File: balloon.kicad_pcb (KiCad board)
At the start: 2 copper layers, 100 x 100 mm, 94 parts, among them J1 USB_B_Micro, J2 Conn_01x06_Socket, J3 Conn_01x06_Socket, J4 Conn_01x02_Socket, J5 Writing Connector, J6 Micro_SD_Card_Det_Hirose_DM3AT, Q1 BSS138, Q2 2SJ681, Q3 BSS138, SW1 DTS-63-F-N-V-RED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

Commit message: replace PCB
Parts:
- removed REF** (x3): MountingHole_3.2mm_M3, MountingHole:MountingHole_3.2mm_M3
- added G***: LOGO, balloon:PQ_LOGO, B.Cu at (53.2, 64.2)
- added H1: MountingHole, MountingHole:MountingHole_3.2mm_M3_ISO7380, F.Cu at (27.8, 49.9)
- added H2: MountingHole, MountingHole:MountingHole_3.2mm_M3_ISO7380, F.Cu at (27.8, 141.5)
- added H3: MountingHole, MountingHole:MountingHole_3.2mm_M3_ISO7380, F.Cu at (119.6, 50.0)
- added J7: Conn_01x06_Socket, Connector_PinHeader_2.54mm:PinHeader_1x06_P2.54mm_Vertical, F.Cu at (45.6, 143.7)
- added J8: Bypass, Connector_PinSocket_2.54mm:PinSocket_1x02_P2.54mm_Vertical, F.Cu at (88.4, 50.5)
- U1: footprint Package_SO:MSOP-10_3x3mm_P0.5mm -> Package_SO:SOP-8_3.9x4.9mm_P1.27mm
- moved J5 55.4 mm to (27.1, 86.3)
- moved J3 17.5 mm to (64.4, 143.7), turned to -90 degrees
- moved J2 14.3 mm to (61.9, 137.3), turned to -90 degrees
- moved C1 1.88 mm to (38.8, 122.7)
- moved U1 0.94 mm to (33.8, 123.7)
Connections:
- J2 pad 3: /PB12 -> /PA0
- J2 pad 4: /PB13 -> /PA7
- J2 pad 5: /PB14 -> /PB0
- J2 pad 6: /PB15 -> GND1
- J3 pad 1: /PC0 -> /I2C3_SDA
- J3 pad 2: /PC1 -> /I2C3_SCL
- J3 pad 3: /PA0 -> unconnected-(J3-Pin_3-Pad3)
- J3 pad 4: /PA7 -> unconnected-(J3-Pin_4-Pad4)
- J3 pad 5: /PA15 -> GND1
- J3 pad 6: /PB0 -> +3V3
- U5 pad 33: /PB12 -> /SPI2_NSS
- U5 pad 34: /PB13 -> /SPI2_SCK
- U5 pad 35: /PB14 -> /SPI2_MISO
- U5 pad 36: /PB15 -> /SPI2_MOSI
- U5 pad 8: /PC0 -> /I2C3_SCL
- U5 pad 9: /PC1 -> /I2C3_SDA
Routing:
- net GND1: track 603.2 -> 0.00 mm, vias 245 -> 303
- net /USART3_TX: track 79.9 -> 161.3 mm
- net /SWCLK: track 10.2 -> 86.6 mm, vias 0 -> 2
- net /SWO: track 17.5 -> 72.2 mm, vias 0 -> 1
- net /I2C3_SCL: track 0.00 -> 54.4 mm, vias 0 -> 2
- net /SWDIO: track 21.5 -> 72.1 mm, vias 1 -> 3
- net +3V3: track 191.4 -> 240.8 mm, vias 1 -> 3
- net /SPI2_SCK: track 0.00 -> 47.5 mm, vias 0 -> 1
- net /BOOT0: track 57.1 -> 103.0 mm, vias 2 -> 1
- net /PC0: track 45.6 -> 0.00 mm, vias 1 -> 0
- net Net-(BT2--): track 18.5 -> 61.8 mm, vias 0 -> 1
- net /PC1: track 42.9 -> 0.00 mm, vias 1 -> 0
- net /I2C3_SDA: track 0.00 -> 42.3 mm, vias 0 -> 2
- net /USART3_RX: track 86.4 -> 128.6 mm, vias 2 -> 1
- net /SPI2_NSS: track 0.00 -> 37.7 mm, vias 0 -> 1
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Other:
- board text added: "1"
- board text added: "2024 PQ-Balloon"
- board text added: "3V3"
- board text added: "AE_BNO280"
- board text added: "BNO055"
- board text added: "DNP"
- board text added: "GND"
- board text added: "GNSS"
- board text added: "MISO"
- board text added: "MOSI"
- board text added: "NRST"
- board text added: "ON"
- board text added: "RM92"
- board text added: "SCL"
- board text added: "SDA"
- board text added: "SS"
- board text added: "SWCLK"
- board text added: "SWDIO"
- board text added: "SWO"

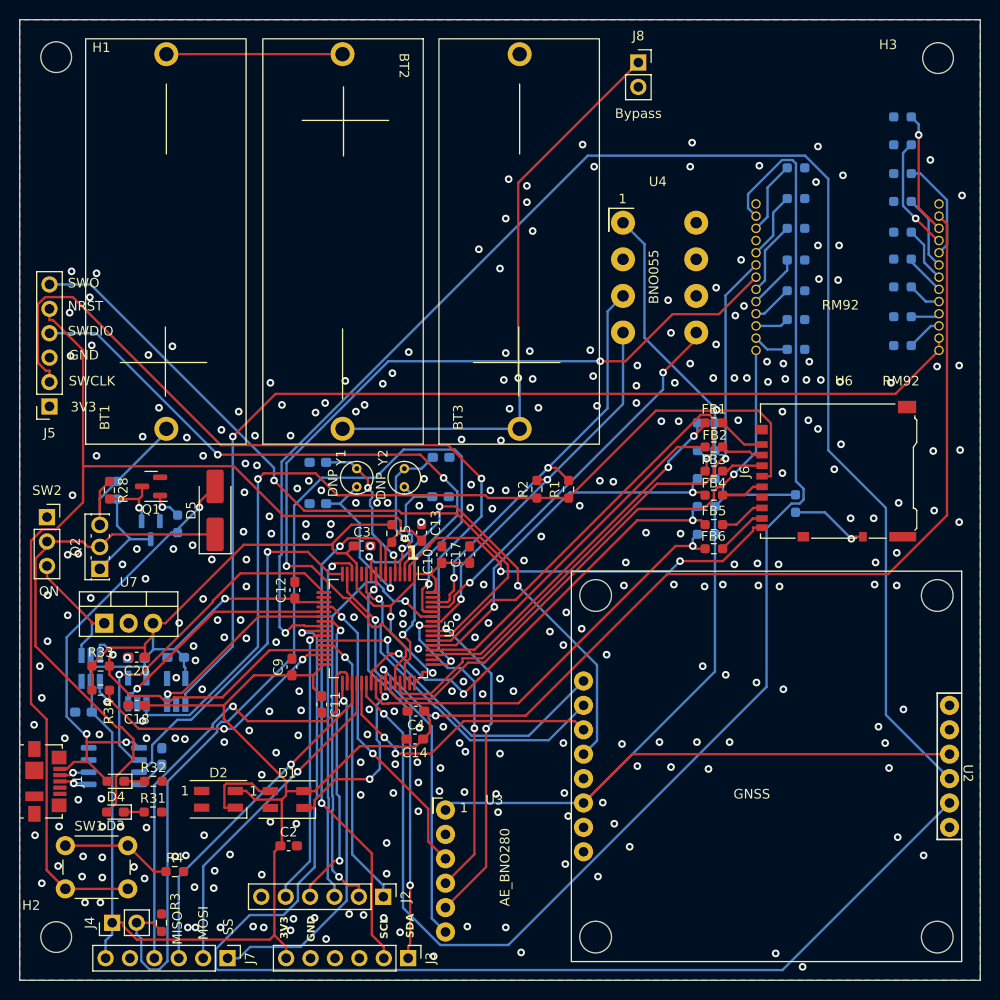
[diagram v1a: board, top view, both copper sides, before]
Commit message: add stmcube
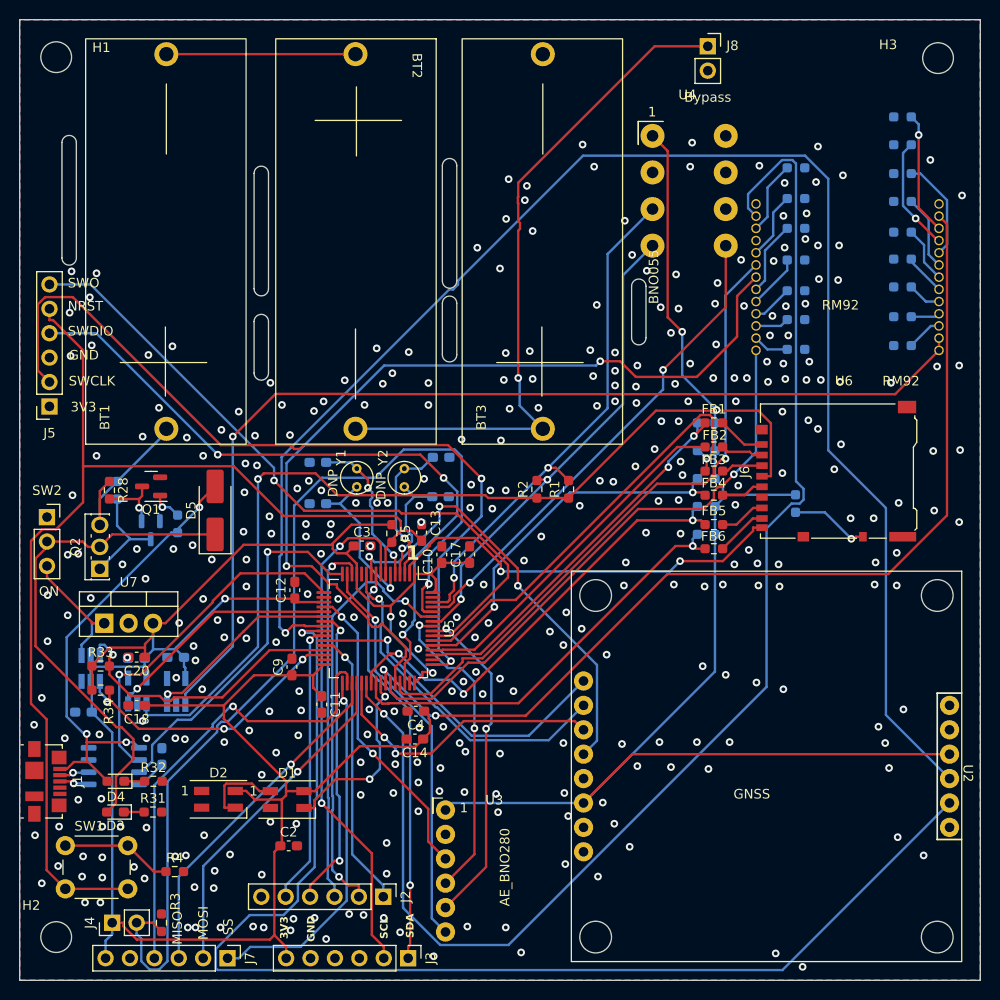
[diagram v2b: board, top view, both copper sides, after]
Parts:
- moved G*** 70.1 mm to (103.2, 113.3), turned to 90 degrees
- moved U4 9.55 mm to (93.6, 63.0)
- moved J8 7.43 mm to (95.6, 48.8)
- moved BT3 2.41 mm to (78.4, 69.2)
- moved BT2 1.35 mm to (59.1, 69.0)
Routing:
- net /I2C1_SDA: track 43.6 -> 54.0 mm
- net /I2C1_SCL: track 39.9 -> 50.2 mm
- net /BNO055_RESET: track 41.0 -> 51.3 mm
- net Net-(BT2--): track 61.8 -> 72.0 mm
- net /PowerSource/VSENSE: track 232.0 -> 239.8 mm, vias 2 -> 3
- net /USART1_CTS: track 88.2 -> 92.2 mm
- net Net-(BT1--): track 18.3 -> 19.7 mm
- net /USART3_TX: track 161.3 -> 161.8 mm
- net GND1: vias 303 -> 340
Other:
- outline, holes or cut-outs redrawn

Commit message: change gnss
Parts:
- removed U2: Qwiic-SAM-M8Q, balloon:Qwiic_SAM-M8Q
- added C21: 100n, Capacitor_SMD:C_0603_1608Metric_Pad1.08x0.95mm_HandSolder, F.Cu at (106.3, 129.0)
- added C22: 100n, Capacitor_SMD:C_0603_1608Metric_Pad1.08x0.95mm_HandSolder, F.Cu at (103.6, 112.5)
- added C23: 100n, Capacitor_SMD:C_0603_1608Metric_Pad1.08x0.95mm_HandSolder, F.Cu at (106.4, 112.5)
- added D6: SMBJ45CA, Diode_SMD:D_SMB, F.Cu at (100.6, 134.3)
- added D7: D, Diode_SMD:D_SMA_Handsoldering, F.Cu at (102.9, 107.6)
- added H4: MountingHole, MountingHole:MountingHole_3.2mm_M3_ISO7380, F.Cu at (119.6, 141.5)
- added J9: Conn_Coaxial, Connector_Coaxial:SMA_Amphenol_132291_Vertical, F.Cu at (103.7, 140.9)
- added L1: BLM18PG471SN1D, Resistor_SMD:R_0603_1608Metric_Pad0.98x0.95mm_HandSolder, F.Cu at (104.6, 131.1)
- added R35: 100, Resistor_SMD:R_0603_1608Metric_Pad0.98x0.95mm_HandSolder, F.Cu at (108.1, 131.1)
- added R36: 1k, Resistor_SMD:R_0603_1608Metric_Pad0.98x0.95mm_HandSolder, F.Cu at (99.3, 112.5)
- added U11: MAX-M10S, RF_GPS:ublox_MAX, F.Cu at (107.1, 121.3)
- C10, C11, C12, C13, C14, C17, C3, C4, C9, R5, U5: moved to B.Cu
- G***: moved to F.Cu
- R30: value 10k -> 47k
- moved G*** 33.1 mm to (70.7, 106.8), turned to 0 degrees
- moved R16 28.6 mm to (116.8, 54.4), turned to 180 degrees
- moved R18 27.1 mm to (105.7, 54.8), turned to 0 degrees
- moved C12 25.5 mm to (73.9, 119.4), turned to 0 degrees
- moved R10 24.7 mm to (105.7, 78.6), turned to 0 degrees
- moved R17 23.1 mm to (116.8, 57.5), turned to 180 degrees
- moved C3 22.2 mm to (78.5, 112.4), turned to 90 degrees
- moved R19 21.7 mm to (105.7, 57.8), turned to 0 degrees
- moved R5 19.7 mm to (79.8, 109.3), turned to 180 degrees
- moved R11 19.5 mm to (105.7, 75.7), turned to 0 degrees
- moved R9 18.2 mm to (116.8, 60.5), turned to 180 degrees
- moved R6 16.9 mm to (116.8, 73.3), turned to 180 degrees
- moved R20 16.5 mm to (105.7, 60.9), turned to 0 degrees
- moved C13 15.6 mm to (79.9, 106.2), turned to 0 degrees
- moved C14 15.5 mm to (58.4, 106.9), turned to -90 degrees
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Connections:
- net /PowerSource/VSENSE renamed /MAX-M10S/VIN
- net /RM92A_RESEST renamed /RM92A_RESET
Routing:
- net /USART3_TX: track 161.8 -> 47.6 mm
- net /USART3_RX: track 128.6 -> 50.3 mm
- net /USART1_RX: track 61.0 -> 126.8 mm, vias 1 -> 2
- net /RM92A_RESET: track 141.7 -> 92.5 mm, vias 1 -> 2
- net /USART2_TX: track 38.2 -> 86.8 mm, vias 1 -> 0
- net /GPS_SAFE: track 30.2 -> 75.0 mm, vias 2 -> 1
- net /SWCLK: track 86.7 -> 47.9 mm, vias 2 -> 1
- net /PB7: track 44.6 -> 82.9 mm
- net /I2C1_SDA: track 54.0 -> 91.0 mm, vias 2 -> 0
- net /MAX-M10S/VIN: track 239.8 -> 272.8 mm, vias 3 -> 2
- net /SPI1_MISO: track 34.5 -> 65.2 mm
- net /BOOT0: track 103.0 -> 72.5 mm, vias 1 -> 0
- net /OSC32_IN: track 15.6 -> 36.4 mm, vias 1 -> 3
- net /USART1_CTS: track 92.2 -> 110.9 mm, vias 2 -> 1
- net +3V3: track 240.8 -> 259.3 mm, vias 3 -> 4
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
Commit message: add icon
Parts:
- moved G*** 4.47 mm to (70.3, 111.3)

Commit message: change conn
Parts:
- added J10: Conn_01x03_Socket, Connector_PinHeader_2.54mm:PinHeader_1x03_P2.54mm_Vertical, F.Cu at (121.1, 110.4)
- J9: footprint Connector_Coaxial:SMA_Amphenol_132291_Vertical -> Connector_Coaxial:U.FL_Hirose_U.FL-R-SMT-1_Vertical
- L1: footprint Resistor_SMD:R_0603_1608Metric_Pad0.98x0.95mm_HandSolder -> Resistor_SMD:R_0402_1005Metric_Pad0.72x0.64mm_HandSolder
- moved C21 0.82 mm to (107.1, 129.2)
- moved L1 0.22 mm to (104.4, 131.0)
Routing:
- net /USART3_TX: track 47.6 -> 62.5 mm
- net /USART3_RX: track 50.3 -> 63.0 mm
- net Net-(D6-A2): track 16.0 -> 17.1 mm
- net Net-(C21-Pad1): track 3.81 -> 4.55 mm
- net GND1: vias 271 -> 303

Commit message: set gerber
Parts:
- moved Q2 2.20 mm to (31.1, 101.3)
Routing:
- net Net-(BT1-+): track 17.8 -> 15.4 mm
- net Net-(D3-A): track 51.9 -> 53.5 mm
- net Net-(Q2-G): track 11.3 -> 12.1 mm
- net GND1: vias 303 -> 311

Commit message: change schematics
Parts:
- removed the G*** at (70.3, 111.3)
- added G***: LOGO, LOGO, F.Cu at (73.4, 112.5)
- added J11: Conn_01x06_Socket, Connector_PinHeader_2.54mm:PinHeader_1x06_P2.54mm_Vertical, F.Cu at (120.9, 117.2)
- H1, H2, H3, H4: footprint MountingHole:MountingHole_3.2mm_M3_ISO7380 -> MountingHole:MountingHole_3.2mm_M3_ISO7380_Pad_TopBottom
- SW1: footprint Button_Switch_THT:SW_PUSH_6mm -> Button_Switch_SMD:SW_SPST_PTS645
- moved SW1 4.01 mm to (32.1, 134.2)
- moved J10 2.72 mm to (121.0, 107.7)
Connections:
- net Net-(J1-D+) renamed /USBD+
- net Net-(J1-D-) renamed /USBD-
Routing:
- net /USART3_TX: track 62.5 -> 91.1 mm
- net /MAX-M10S/VIN: track 272.8 -> 293.5 mm, vias 2 -> 4
- net /USART3_RX: track 63.0 -> 82.2 mm
- net /USBD+: track 3.64 -> 3.12 mm
- net /NRST: track 124.5 -> 124.7 mm, vias 2 -> 3
- net GND1: vias 311 -> 326
